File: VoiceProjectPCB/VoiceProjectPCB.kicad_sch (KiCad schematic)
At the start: 69 parts, among them J1 Conn_01x02_Socket, J2 Conn_01x02_Socket, J3 217B-CA04, J4 Conn_01x06_Socket, J5 Conn_01x06_Socket, J6 Screw_Terminal_01x02, SW3 SW_Push, SW4 SW_Push, U1 PAM8406D, U2 PAM8406D, U4 ESP32-WROOM-E, U5 AMS1117-3.3, U6 PCM5102A

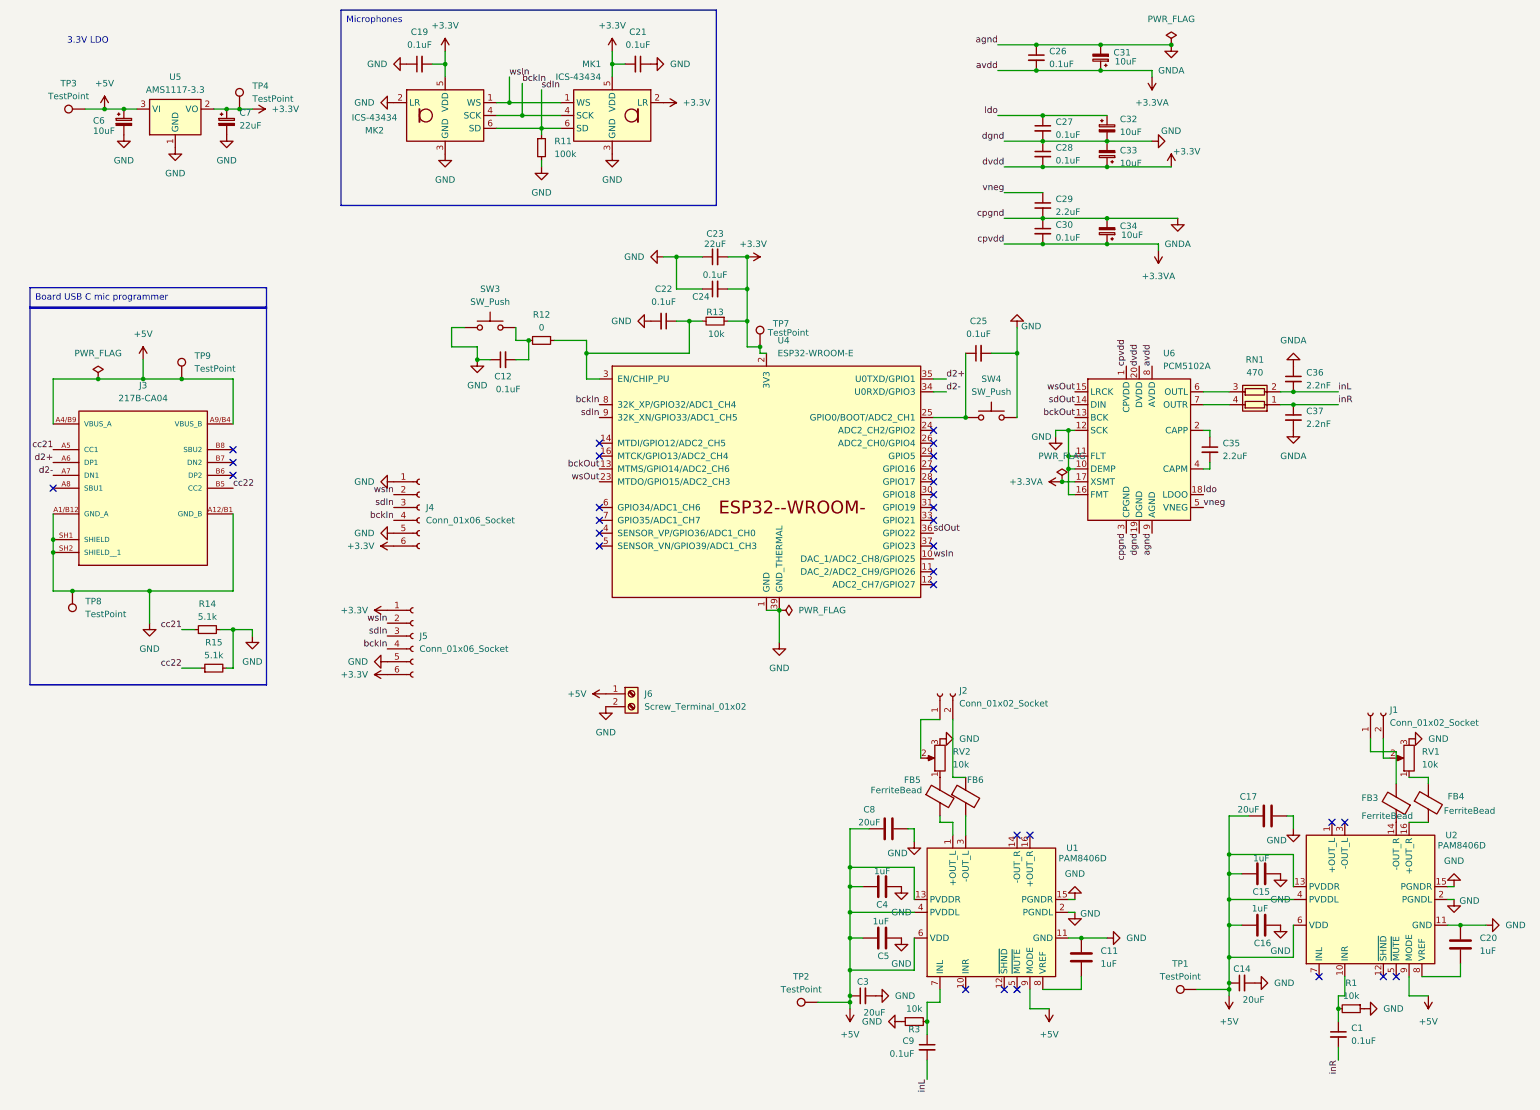
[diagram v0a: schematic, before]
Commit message: Mk 2 PCB, Switched to DSP for Voice Modulation
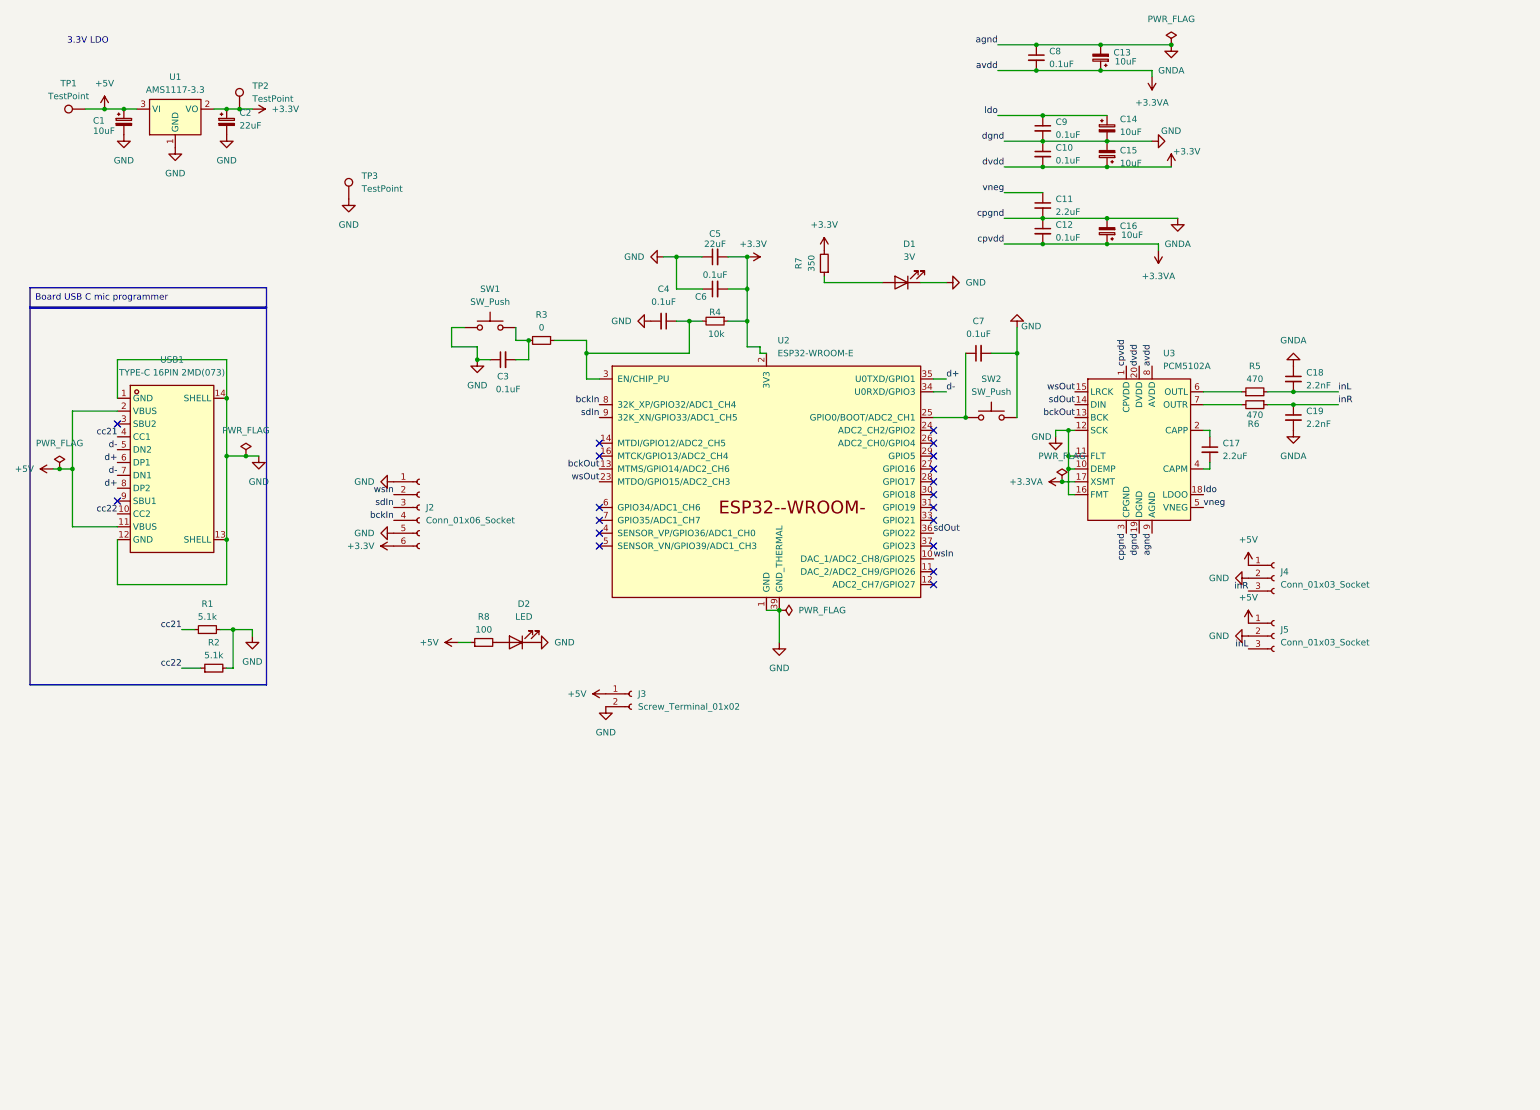
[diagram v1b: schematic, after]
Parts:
- removed C1, C19, C21, C9: 0.1uF, Capacitor_SMD:C_0805_2012Metric, symbol Device:C_Small
- removed C11, C15, C16, C20, C4, C5: 1uF, Capacitor_SMD:C_0805_2012Metric, symbol Device:C
- removed C14, C3: 20uF, Capacitor_SMD:C_1812_4532Metric, symbol Device:C_Small
- removed C17, C8: 20uF, Capacitor_SMD:C_1812_4532Metric, symbol Device:C
- removed FB3, FB4, FB5, FB6: FerriteBead, Inductor_SMD:L_0603_1608Metric, symbol Device:FerriteBead
- removed J1, J2: Conn_01x02_Socket, Connector_JST:JST_EH_B2B-EH-A_1x02_P2.50mm_Vertical, symbol Connector:Conn_01x02_Socket
- removed J3: 217B-CA04, 217B_CA04 (1):ATTEND_217B-CA04, symbol receptacle:217B-CA04
- removed J5: Conn_01x06_Socket, Connector_JST:JST_EH_B6B-EH-A_1x06_P2.50mm_Vertical, symbol Connector:Conn_01x06_Socket
- removed MK1, MK2: ICS-43434, Sensor_Audio:InvenSense_ICS-43434-6_3.5x2.65mm, symbol Sensor_Audio:ICS-43434
- removed R1, R3: 10k, Resistor_SMD:R_0805_2012Metric, symbol Device:R_Small
- removed R11: 100k, Resistor_SMD:R_0805_2012Metric, symbol Device:R_Small
- removed RN1: 470, Resistor_SMD:R_Array_Convex_2x0606, symbol Device:R_Pack02
- removed RV1, RV2: 10k, 3310P_025_103L:POT_3310P-025-103L, symbol Device:R_Potentiometer
- removed TP1, TP2: TestPoint, TestPoint:TestPoint_Pad_D1.5mm, symbol Connector:TestPoint
- removed TP7, TP8, TP9: TestPoint, TestPoint:TestPoint_Plated_Hole_D2.0mm, symbol Connector:TestPoint
- removed U1, U2: PAM8406D, Package_SO:SOP-16_3.9x9.9mm_P1.27mm, symbol Amplifier_Audio:PAM8406D
- added D1: 3V, LED_SMD:LED_0603_1608Metric, symbol Device:LED
- added D2: LED, LED_SMD:LED_0603_1608Metric, symbol Device:LED
- added J4, J5: Conn_01x03_Socket, B3B_XH_A:JST_B3B-XH-A, symbol Connector:Conn_01x03_Socket
- added R5, R6: 470, Resistor_SMD:R_0402_1005Metric, symbol Device:R_Small
- added R7: 350, Resistor_SMD:R_0402_1005Metric, symbol Device:R_Small
- added R8: 100, Resistor_SMD:R_0402_1005Metric, symbol Device:R_Small
- added TP3: TestPoint, TestPoint:TestPoint_Pad_D1.5mm, symbol Connector:TestPoint
- added USB1: TYPE-C 16PIN 2MD(073), easyeda2kicad:USB-C-SMD_TYPE-C-6PIN-2MD-073, symbol easyeda2kicad:TYPE-C16PIN2MD(073)
- C1: renamed from C6; footprint Capacitor_SMD:C_0805_2012Metric -> Capacitor_SMD:C_0402_1005Metric
- C10: renamed from C28; footprint Capacitor_SMD:C_0805_2012Metric -> Capacitor_SMD:C_0402_1005Metric
- C11: renamed from C29; footprint Capacitor_SMD:C_0805_2012Metric -> Capacitor_SMD:C_0402_1005Metric
- C12: renamed from C30; footprint Capacitor_SMD:C_0805_2012Metric -> Capacitor_SMD:C_0402_1005Metric
- C13: renamed from C31; footprint Capacitor_SMD:C_0805_2012Metric -> Capacitor_SMD:C_0402_1005Metric
- C14: renamed from C32; footprint Capacitor_SMD:C_0805_2012Metric -> Capacitor_SMD:C_0402_1005Metric
- C15: renamed from C33; footprint Capacitor_SMD:C_0805_2012Metric -> Capacitor_SMD:C_0402_1005Metric
- C16: renamed from C34; footprint Capacitor_SMD:C_0805_2012Metric -> Capacitor_SMD:C_0402_1005Metric
- C17: renamed from C35; footprint Capacitor_SMD:C_0805_2012Metric -> Capacitor_SMD:C_0805_2012Metric_Pad1.18x1.45mm_HandSolder
- C18: renamed from C36; footprint Capacitor_SMD:C_0805_2012Metric -> Capacitor_SMD:C_0402_1005Metric
- C19: renamed from C37; footprint Capacitor_SMD:C_0805_2012Metric -> Capacitor_SMD:C_0402_1005Metric
- C2: renamed from C7; footprint Capacitor_SMD:C_0805_2012Metric -> Capacitor_SMD:C_0402_1005Metric
- C3: renamed from C12; footprint Capacitor_SMD:C_0805_2012Metric -> Capacitor_SMD:C_0402_1005Metric
- C4: renamed from C22; footprint Capacitor_SMD:C_0805_2012Metric -> Capacitor_SMD:C_0402_1005Metric
- C5: renamed from C23; footprint Capacitor_SMD:C_0805_2012Metric -> Capacitor_SMD:C_0805_2012Metric_Pad1.18x1.45mm_HandSolder
- C6: renamed from C24; footprint Capacitor_SMD:C_0805_2012Metric -> Capacitor_SMD:C_0805_2012Metric_Pad1.18x1.45mm_HandSolder
- C7: renamed from C25; footprint Capacitor_SMD:C_0805_2012Metric -> Capacitor_SMD:C_0402_1005Metric
- C8: renamed from C26; footprint Capacitor_SMD:C_0805_2012Metric -> Capacitor_SMD:C_0402_1005Metric
- C9: renamed from C27; footprint Capacitor_SMD:C_0805_2012Metric -> Capacitor_SMD:C_0402_1005Metric
- J2: renamed from J4; footprint Connector_JST:JST_EH_B6B-EH-A_1x06_P2.50mm_Vertical -> B6B_XH_A:JST_B6B-XH-A
- J3: renamed from J6; footprint ScrewTerminal:CONN_1725672_PXC -> B2B_XH_A:JST_B2B-XH-A; symbol Connector:Screw_Terminal_01x02 -> Connector:Conn_01x02_Socket
- R1: renamed from R14; footprint Resistor_SMD:R_0805_2012Metric -> Resistor_SMD:R_0402_1005Metric
- R2: renamed from R15; footprint Resistor_SMD:R_0805_2012Metric -> Resistor_SMD:R_0402_1005Metric
- R3: renamed from R12; footprint Resistor_SMD:R_0805_2012Metric -> Resistor_SMD:R_0402_1005Metric
- R4: renamed from R13; footprint Resistor_SMD:R_0805_2012Metric -> Resistor_SMD:R_0402_1005Metric
- renumbered SW3 to SW1, SW4 to SW2, TP3 to TP1, TP4 to TP2, U5 to U1, U4 to U2, U6 to U3
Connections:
- net +3.3V: now also R7.2
- net +5V: now also J4.1 (Pin_1), J5.1 (Pin_1), R8.1, USB1.11 (VBUS), USB1.2 (VBUS)
- net GND: now also D1.1 (K), D2.1 (K), J4.2 (Pin_2), J5.2 (Pin_2), TP3.1, USB1.1 (GND), USB1.12 (GND), USB1.13 (SHELL), USB1.14 (SHELL)
- net cc21: now also USB1.4 (CC1)
- net cc22: now also USB1.10 (CC2)
- net inL: now also J5.3 (Pin_3), R5.2
- net inR: now also J4.3 (Pin_3), R6.1
- net at U3.6 (OUTL): now also R5.1
- net at U3.7 (OUTR): now also R6.2
- net d2+ renamed d+
- net d+: now also USB1.6 (DP1), USB1.8 (DP2)
- net d2- renamed d-
- net d-: now also USB1.5 (DN2), USB1.7 (DN1)
- new net: D1.2 (A), R7.1
- new net: D2.2 (A), R8.2
- no-connect marks 31 -> 19
